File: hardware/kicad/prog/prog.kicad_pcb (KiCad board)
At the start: 4 copper layers, 174 x 134 mm, 123 parts, among them J1 AES_PROG, J2 Câble PROG-CHA, J3 CONF P, J4 CONF V, U1 AMS1117-3.3, U10 iCE40HX4K-TQ144, U11 W9825G6KH-6, U12 iCE40HX4K-TQ144, U13 W9825G6KH-6, U2 AP2112K-1.2, U3 74LVC16244A, U4 74LVC16244A, U5 74LVC16244A, U6 74LVC16245A, U7 74LVC16245A, U8 74AHCT125, U9 74LVC1G07, X1 25 MHz 3,3 V, X2 25 MHz 3,3 V

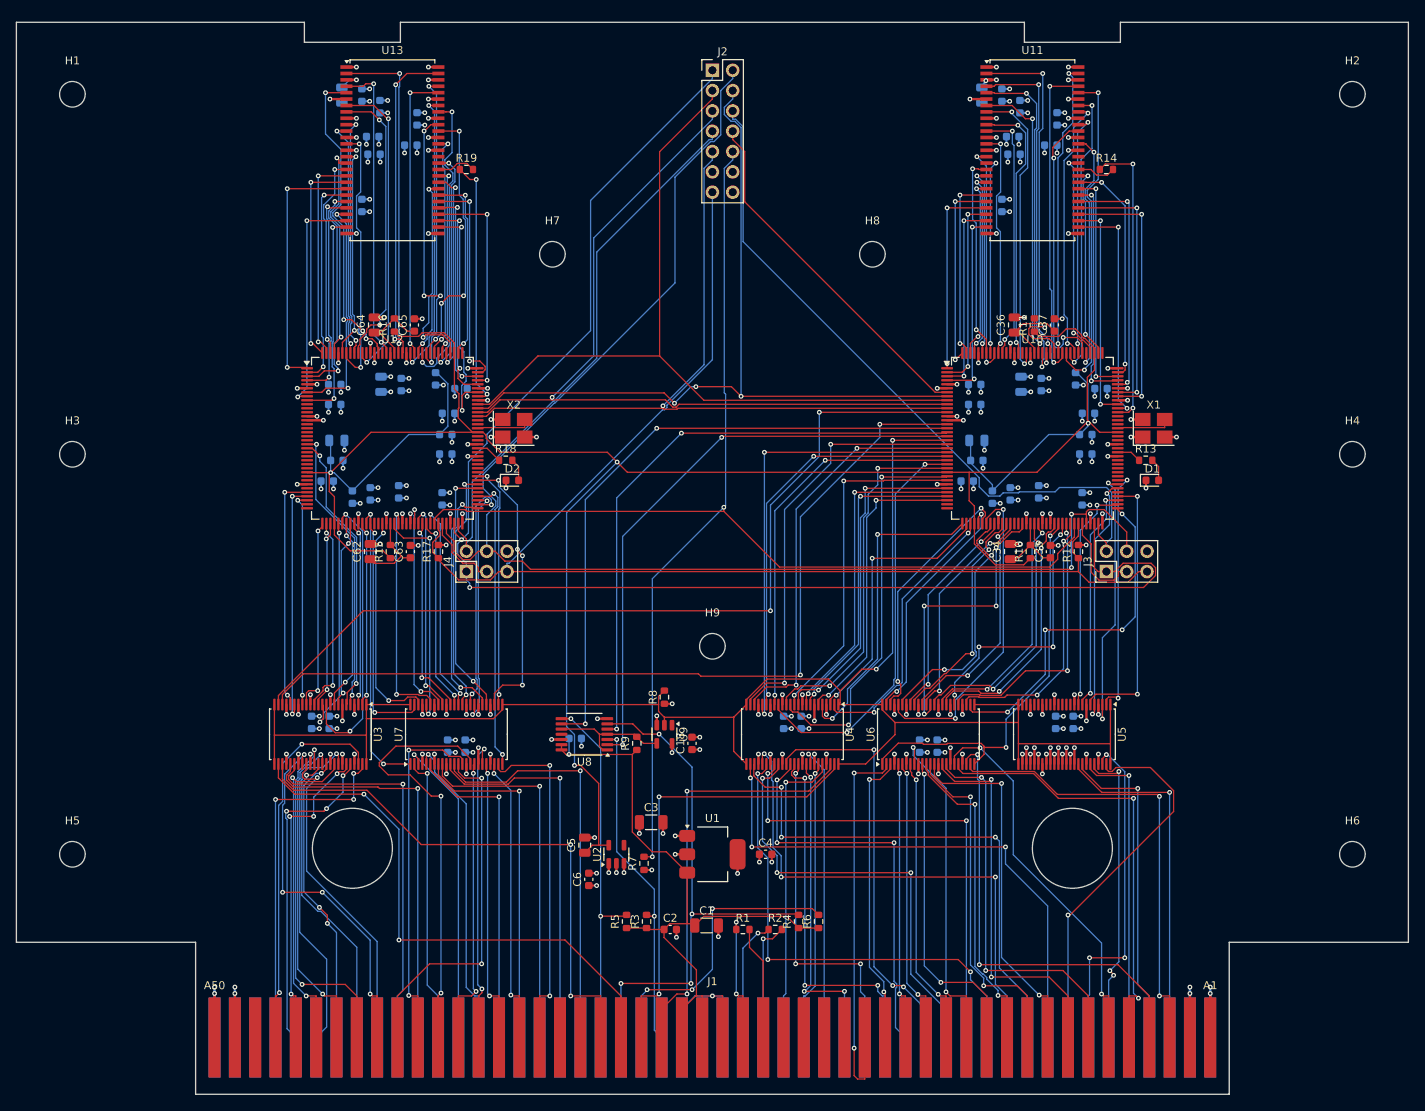
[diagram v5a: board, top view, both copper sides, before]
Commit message: Pico 2, microSD et bouton sur la carte PROG ; pistes d'alimentation larges
- La carte PROG est côté avant de la cartouche, composants vers l'avant :
  lecteur microSD et bouton accessibles. Le câble PROG-CHA porte
  désormais le bus de liaison C/SM ; connecteur au même endroit sur les
  deux cartes (x = 172 mm), prêt pour un connecteur carte à carte.
- Sous le Pico : ni piste ni via sur la face composants (pastilles de
  test nues sous le module).
- Classes de réseaux écrites dans le .kicad_pro : +5V et VSYS en 0,5 mm,
  +1V2 en 0,3 mm.
- Broches des FPGA réoptimisées ; contrôle Freerouting sans violation ;
  routage des deux cartes et vérification de timing en cours.

Co-Authored-By: Claude Opus 5.5 <noreply@anthropic.com>
Claude-Session: https://claude.ai/code/session_01WKfXP1YJ8otGxZ5dsY6Agh
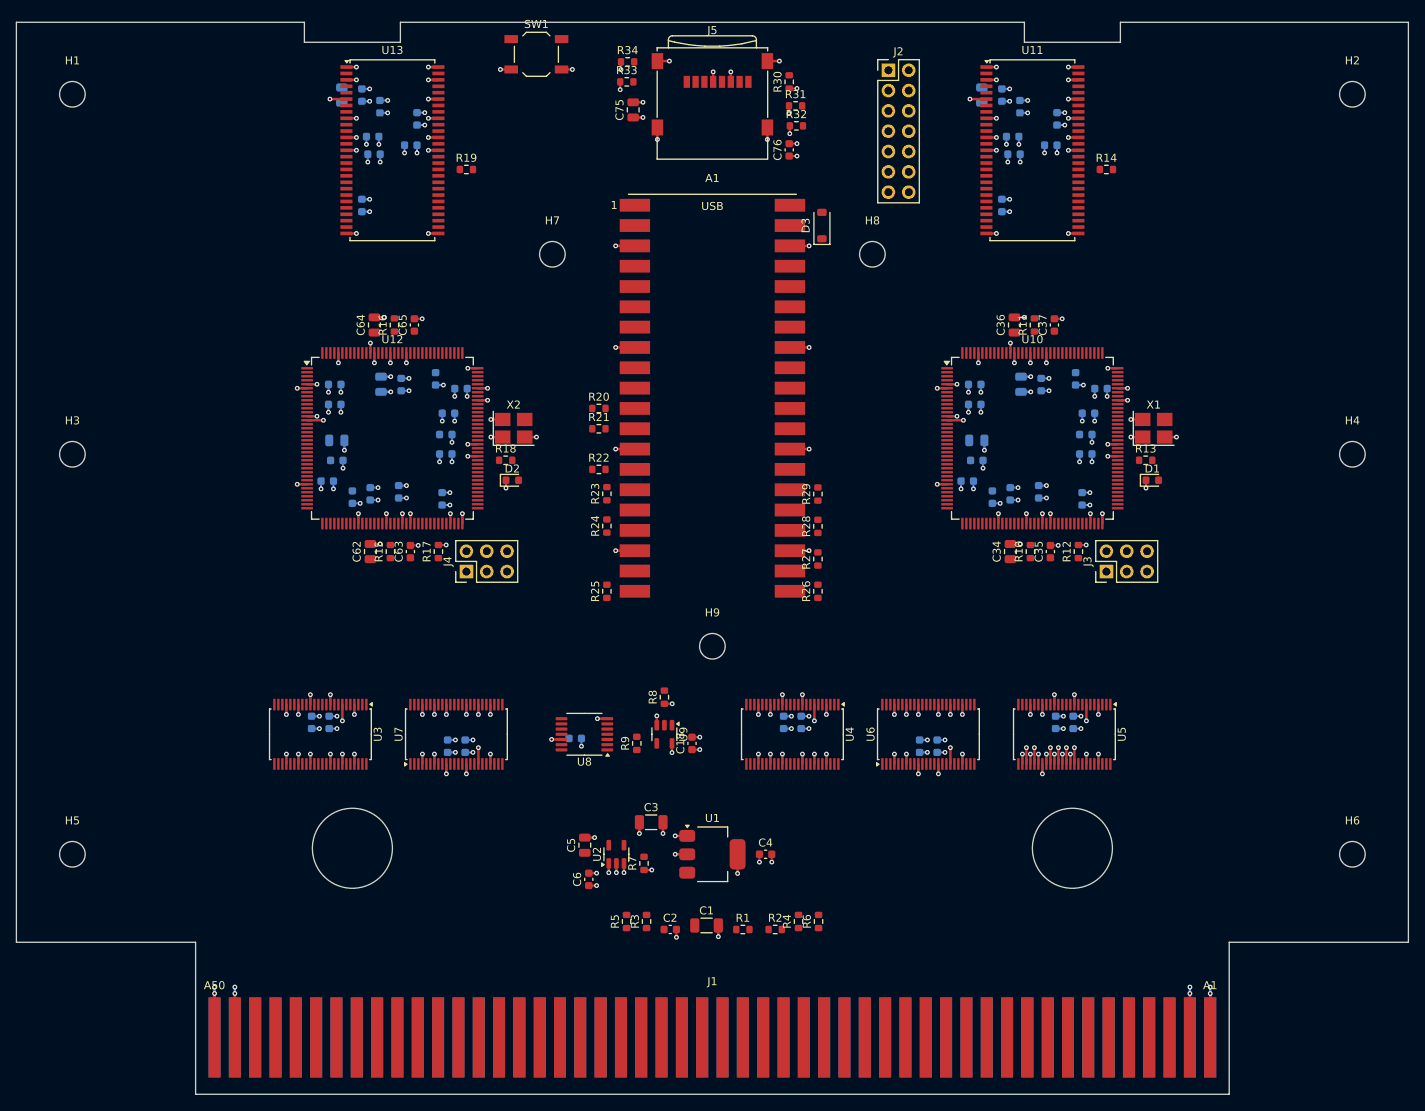
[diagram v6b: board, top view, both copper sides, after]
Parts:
- added A1: Raspberry Pi Pico 2, SDAES:RaspberryPi_Pico2_SMD, F.Cu at (150.0, 93.0)
- added C75: 10u, Capacitor_SMD:C_0805_2012Metric, F.Cu at (140.1, 57.0)
- added C76: 100n, Capacitor_SMD:C_0603_1608Metric, F.Cu at (159.6, 62.0)
- added D3: SS14 / BAT60A, Diode_SMD:D_SOD-123, F.Cu at (163.7, 71.4)
- added J5: microSD, Connector_Card:microSD_HC_Wuerth_693072010801, F.Cu at (150.0, 55.0)
- added R20: 33, Resistor_SMD:R_0603_1608Metric, F.Cu at (135.8, 94.3)
- added R21: 33, Resistor_SMD:R_0603_1608Metric, F.Cu at (135.8, 96.8)
- added R22: 33, Resistor_SMD:R_0603_1608Metric, F.Cu at (135.8, 101.9)
- added R23: 33, Resistor_SMD:R_0603_1608Metric, F.Cu at (136.8, 104.9)
- added R24: 33, Resistor_SMD:R_0603_1608Metric, F.Cu at (136.8, 109.0)
- added R25: 33, Resistor_SMD:R_0603_1608Metric, F.Cu at (136.8, 117.1)
- added R26: 33, Resistor_SMD:R_0603_1608Metric, F.Cu at (163.2, 117.1)
- added R27: 33, Resistor_SMD:R_0603_1608Metric, F.Cu at (163.2, 113.1)
- added R28: 33, Resistor_SMD:R_0603_1608Metric, F.Cu at (163.2, 109.0)
- added R29: 33, Resistor_SMD:R_0603_1608Metric, F.Cu at (163.2, 105.0)
- added R30: 10k, Resistor_SMD:R_0603_1608Metric, F.Cu at (159.6, 53.5)
- added R31: 10k, Resistor_SMD:R_0603_1608Metric, F.Cu at (160.4, 56.5)
- added R32: 10k, Resistor_SMD:R_0603_1608Metric, F.Cu at (160.5, 59.0)
- added R33: 10k, Resistor_SMD:R_0603_1608Metric, F.Cu at (139.3, 53.5)
- added R34: 10k, Resistor_SMD:R_0603_1608Metric, F.Cu at (139.4, 51.0)
- added SW1: Retour menu, Button_Switch_SMD:SW_SPST_TL3342, F.Cu at (128.0, 50.0)
- moved J2 22.0 mm to (172.0, 52.0)
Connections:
- J2 pad 1: PROG_SCK -> CHA_SCK
- J2 pad 2: PROG_IO0 -> CHA_IO0
- J2 pad 3: PROG_IO1 -> CHA_IO1
- J2 pad 4: PROG_IO2 -> CHA_IO2
- J2 pad 5: PROG_IO3 -> CHA_IO3
- J2 pad 6: CS_P -> CS_C
- J2 pad 7: CS_V -> CS_SM
- J2 pad 8: LK_IRQ -> GND
- U10 pad 10: PROG_IO3 -> PROG_IO2
- U10 pad 11: MODE -> PROG_IO3
- U10 pad 7: LK_IRQ -> MODE
- U10 pad 8: PROG_IO2 -> LK_IRQ
- U12 pad 87: (no net) -> V_LED
- U12 pad 88: V_LED -> PROG_IO3
- U12 pad 90: (no net) -> PROG_IO2
- U12 pad 91: (no net) -> PROG_IO1
- U12 pad 96: MODE -> (no net)
- U12 pad 97: PROG_IO3 -> MODE
- U12 pad 98: PROG_IO2 -> (no net)
- U12 pad 99: PROG_IO1 -> (no net)
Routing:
- net +1V2: track 299.3 -> 0.00 mm, vias 4 -> 0
- net XLAT_EN_N: track 215.3 -> 0.00 mm, vias 2 -> 0
- net PROG_SCK: track 182.2 -> 0.00 mm, vias 2 -> 0
- net CDONE: track 181.7 -> 0.00 mm, vias 2 -> 0
- net PROG_IO0: track 176.1 -> 0.00 mm, vias 2 -> 0
- net CRESET_N: track 161.4 -> 0.00 mm
- net +5V: track 112.5 -> 0.00 mm, vias 2 -> 0
- net PORTWEL_N: track 111.1 -> 0.00 mm, vias 2 -> 0
- net PORTWEU_N: track 110.3 -> 0.00 mm, vias 2 -> 0
- net PROG_IO3: track 104.3 -> 0.00 mm, vias 1 -> 0
- net PROG_IO2: track 101.1 -> 0.00 mm, vias 3 -> 0
- net PROG_IO1: track 99.4 -> 0.00 mm
- net MODE: track 93.8 -> 0.00 mm, vias 1 -> 0
- net CS_P: track 89.2 -> 0.00 mm
- net PWAIT1_N: track 79.9 -> 0.00 mm, vias 2 -> 0
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
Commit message: Carte PROG routée avec le Pico 2, la microSD et le bouton
Routage Freerouting, raccordements aux plans et routeur de finition ;
empilement et biseau du connecteur de bord ajoutés.

Co-Authored-By: Claude Opus 5.5 <noreply@anthropic.com>
Claude-Session: https://claude.ai/code/session_01WKfXP1YJ8otGxZ5dsY6Agh
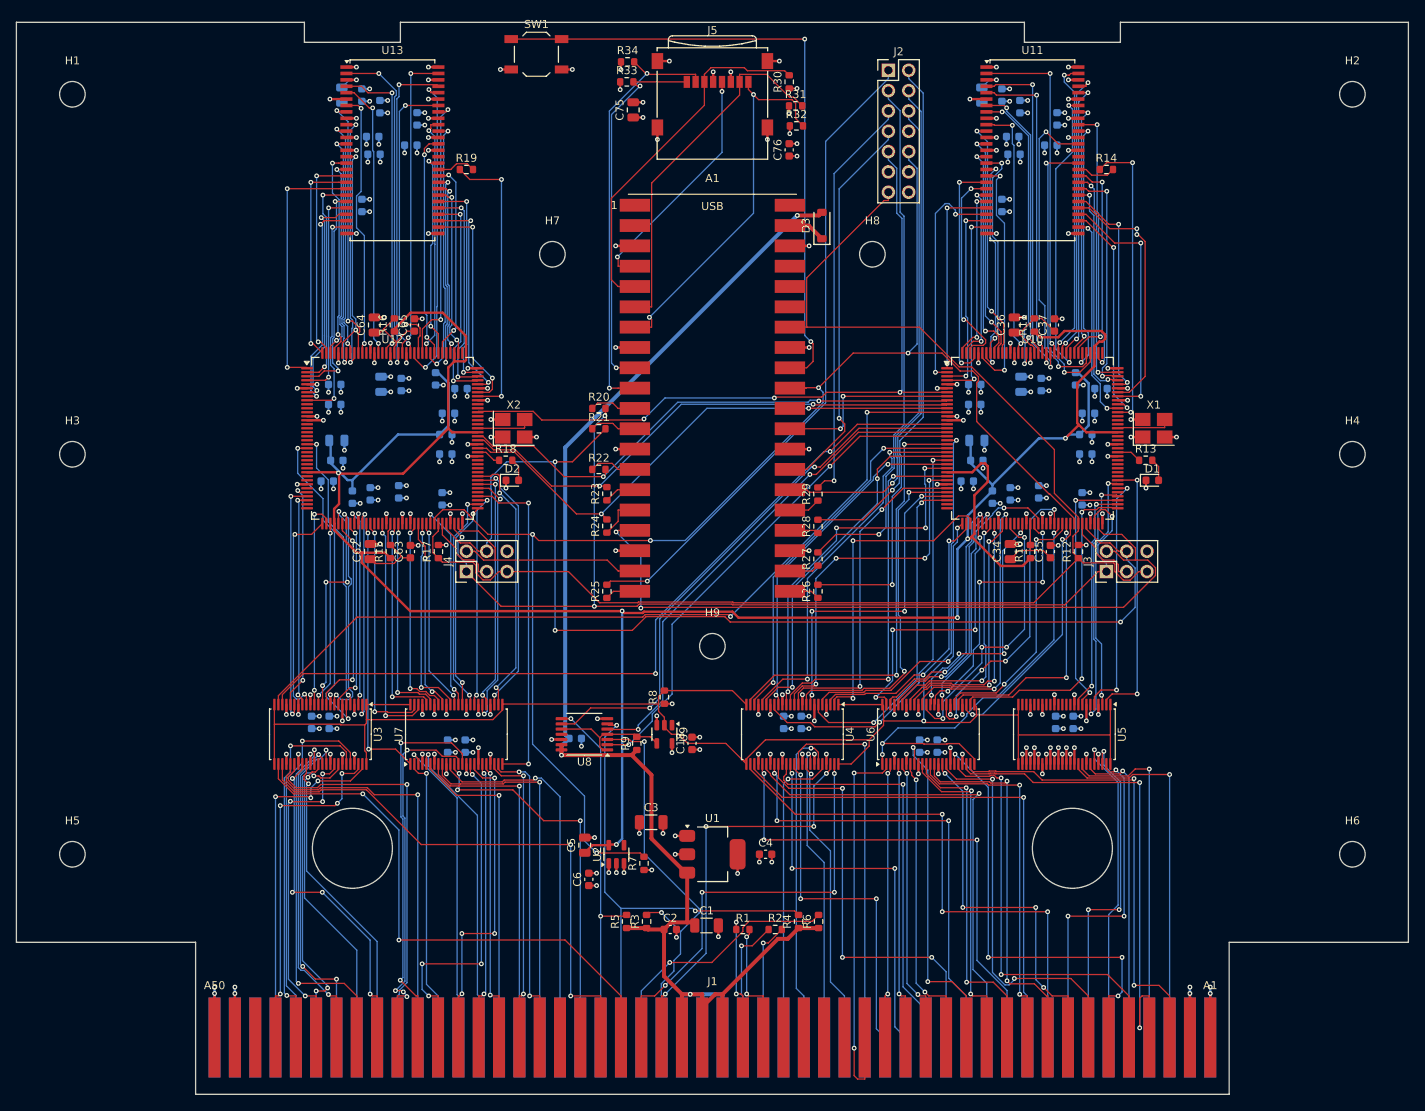
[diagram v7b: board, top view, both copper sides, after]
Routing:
- net +1V2: track 0.00 -> 311.5 mm, vias 0 -> 6
- net XLAT_EN_N: track 0.00 -> 214.0 mm, vias 0 -> 2
- net +5V: track 0.00 -> 196.1 mm, vias 0 -> 3
- net CDONE: track 0.00 -> 186.1 mm, vias 0 -> 5
- net CRESET_N: track 0.00 -> 177.9 mm
- net PROG_IO0: track 0.00 -> 142.9 mm, vias 0 -> 3
- net PROG_SCK: track 0.00 -> 128.0 mm, vias 0 -> 4
- net PORTWEU_N: track 0.00 -> 104.5 mm, vias 0 -> 2
- net PORTWEL_N: track 0.00 -> 102.3 mm, vias 0 -> 2
- net CS_P: track 0.00 -> 95.0 mm, vias 0 -> 2
- net MODE: track 0.00 -> 91.5 mm, vias 0 -> 3
- net CHA_SCK: track 0.00 -> 81.6 mm, vias 0 -> 1
- net BUTTON_N: track 0.00 -> 80.6 mm, vias 0 -> 2
- net CHA_IO0: track 0.00 -> 76.1 mm, vias 0 -> 1
- net AES_PORTWEL: track 0.00 -> 69.4 mm, vias 0 -> 2
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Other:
- board text added: "Contacts de bord : or dur, biseau 45° (chanfrein). Finition ENIG, 4 couches, 1,6 mm."
